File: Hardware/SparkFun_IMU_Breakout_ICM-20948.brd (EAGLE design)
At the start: 25.4 x 25.4 mm, 102 parts, among them Q1 DMN2005LP4K-7, Q10 RE1C002UN, Q11 DMN2005LP4K-7, Q12 RE1C002UN, Q13 DMN2005LP4K-7, Q14 RE1C002UN, Q15 DMN2005LP4K-7, Q16 RE1C002UN, Q2 RE1C002UN, Q3 DMN2005LP4K-7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

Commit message: Laid out v30
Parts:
- removed Q1, Q11, Q13, Q15, Q3, Q5, Q7, Q9: DMN2005LP4K-7, new_fets:AP02001
- added U$28: (no value), SparkFun-Aesthetics:SFE_LOGO_FLAME_.1
- added U$49: (no value), buzzard_labels (1):M3
- added U$50, U$57: (no value), buzzard_labels (1):X0
- added U$51, U$58: (no value), buzzard_labels (1):Y1
- added U$52, U$59: (no value), buzzard_labels (1):Z2
- added U$60: (no value), buzzard_labels (1):G5
- added U$61: (no value), buzzard_labels (1):A4
- moved R25 96.4 mm to (8.89, 18.7)
- moved R19 96.1 mm to (14.0, 18.7)
- moved R21 95.3 mm to (16.5, 18.7)
- moved R20 93.9 mm to (16.5, 15.9), turned to 180 degrees
- moved R23 91.3 mm to (11.4, 18.7)
- moved Q14 89.8 mm to (11.4, 17.8)
- moved R22 89.6 mm to (11.4, 15.9), turned to 180 degrees
- moved Q10 87.3 mm to (14.0, 17.8)
- moved R24 87.0 mm to (8.89, 15.9), turned to 180 degrees
- moved Q16 86.3 mm to (8.89, 17.8)
- moved Q12 85.8 mm to (16.5, 17.8)
- moved R18 84.9 mm to (14.0, 15.9), turned to 180 degrees
- moved R17 66.2 mm to (11.4, 6.73), turned to 180 degrees
- moved Q8 62.9 mm to (11.4, 7.62), turned to 180 degrees
- moved R16 61.7 mm to (11.4, 9.53)
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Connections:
- net AUX_CL_VIN_JMP renamed N$4
- net AUX_DA_VIN_JMP renamed N$5
- net SCL/SCLK_VIN_JMP renamed N$2
- net SDA/SDI_VIN_JMP renamed N$3
- net !CS: no longer Q1.S
- net !CS!_VIN: no longer Q1.D
- net 1.8V: no longer Q1.G, Q11.G, Q13.G, Q15.G, Q3.G, Q5.G, Q7.G, Q9.G
- net AD0/SDO: no longer Q3.S
- net AD0/SDO_VIN: no longer Q3.D
- net AUX_CL: no longer Q11.S
- net AUX_CL_VIN: now also J4.5; no longer J4.3, Q11.D
- net AUX_DA: no longer Q9.S
- net AUX_DA_VIN: now also J4.4; no longer J4.2, Q9.D
- net FSYNC: no longer Q13.S
- net FSYNC_VIN: now also J4.3; no longer J4.4, Q13.D
- net INT: no longer Q15.S
- net INT_VIN: now also J4.2; no longer J4.5, Q15.D
- net SCL/SCLK: no longer Q5.S
- net SCL/SCLK_VIN: no longer Q5.D
- net SDA/SDI: no longer Q7.S
- net SDA/SDI_VIN: no longer Q7.D
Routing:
- net VIN: track 0.00 -> 69.9 mm, vias 0 -> 11
- net 1.8V: track 0.00 -> 55.1 mm, vias 0 -> 11
- net SCL/SCLK_VIN: track 0.00 -> 41.8 mm, vias 0 -> 2
- net SDA/SDI_VIN: track 0.00 -> 41.4 mm, vias 0 -> 2
- net AUX_DA: track 0.00 -> 11.2 mm, vias 0 -> 2
- net AD0/SDO_VIN: track 0.00 -> 11.1 mm, vias 0 -> 2
- net !CS: track 0.00 -> 8.62 mm, vias 0 -> 2
- net AD0/SDO: track 0.00 -> 8.21 mm, vias 0 -> 2
- net !CS!_VIN: track 0.00 -> 7.80 mm, vias 0 -> 1
- net FSYNC_VIN: track 0.00 -> 7.78 mm, vias 0 -> 1
- net INT_VIN: track 0.00 -> 7.47 mm, vias 0 -> 1
- net AUX_DA_VIN: track 0.00 -> 7.37 mm, vias 0 -> 1
- net AUX_CL_VIN: track 0.00 -> 7.25 mm, vias 0 -> 1
- net GND: track 0.00 -> 6.58 mm, vias 0 -> 16
- net SDA/SDI: track 0.00 -> 5.65 mm, vias 0 -> 2
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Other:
- board text added: "v30"
- board text removed: "v21"

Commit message: Ran board design checklist ahead of the review
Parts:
- Q10, Q12, Q14, Q16, Q2, Q4, Q6, Q8: value RE1C002UN -> 20V/0.2A/8MHz/1.2Ω/1Vth; device new_fets:SOT-416FL -> SparkFun-DiscreteSemi:SOT-416FL
- moved U$37 0.40 mm to (4.78, 19.9)
- moved U$38 0.40 mm to (5.79, 19.9)
- moved U$24 0.13 mm to (6.35, 19.8)

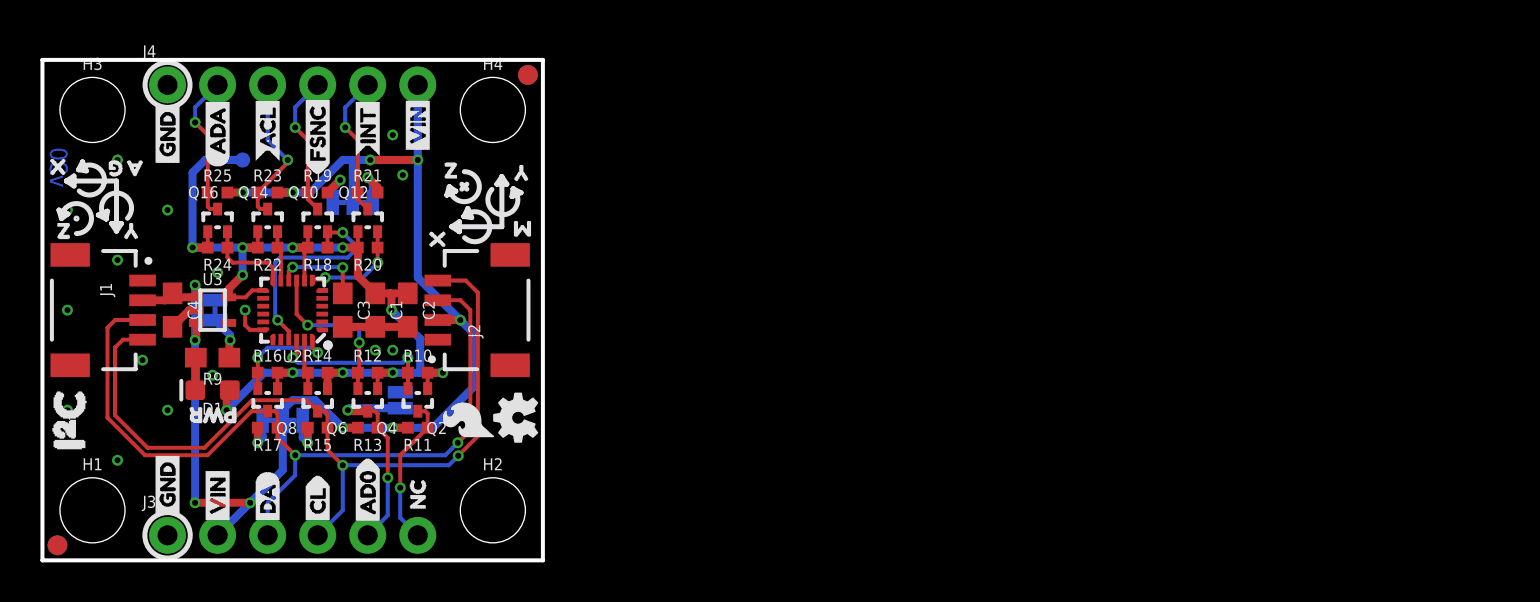
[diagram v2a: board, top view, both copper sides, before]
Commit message: Changes from design review
Level shifter circuit spacing
Axes indicators
Routing touch-ups
LED resistor change
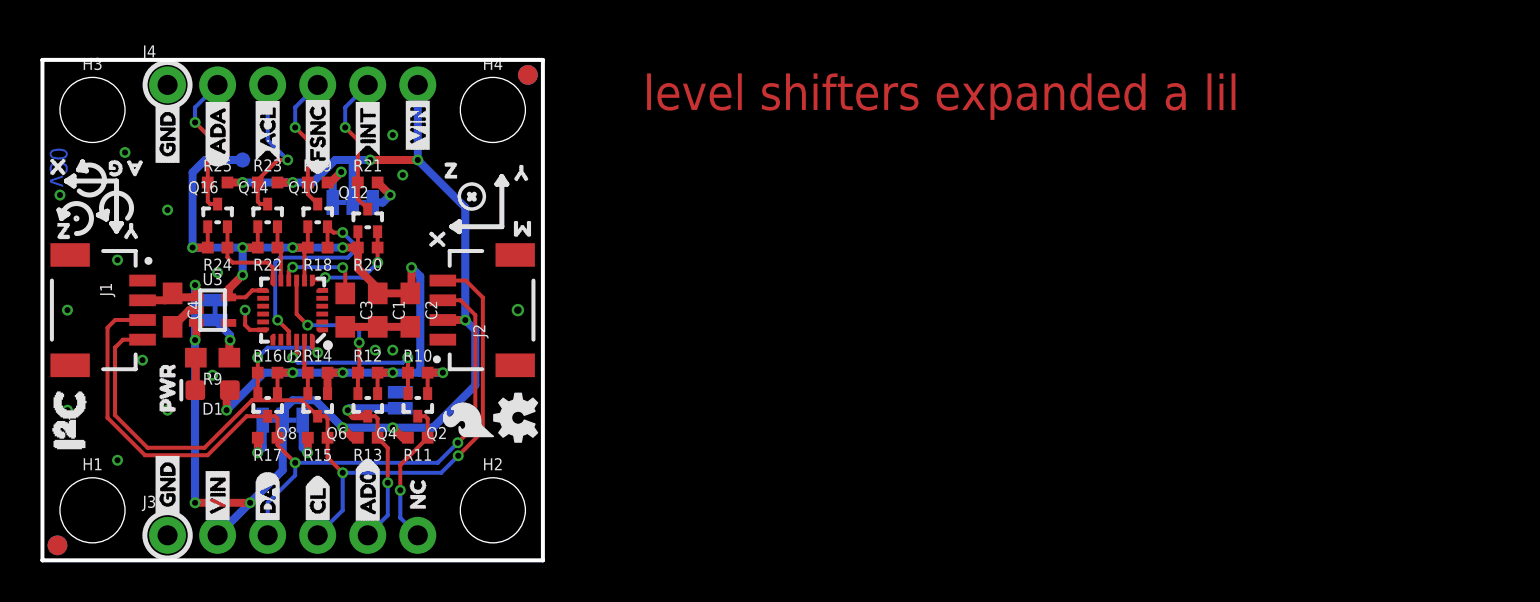
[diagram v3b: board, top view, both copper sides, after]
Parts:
- R9: value 470 -> 220
- moved U$3 4.22 mm to (6.35, 6.86), turned to 90 degrees
- moved R11 0.51 mm to (19.1, 6.22)
- moved R13 0.51 mm to (16.5, 6.22)
- moved R15 0.51 mm to (14.0, 6.22)
- moved R17 0.51 mm to (11.4, 6.22)
- moved R19 0.51 mm to (14.0, 19.2)
- moved R21 0.51 mm to (16.5, 19.2)
- moved R23 0.51 mm to (11.4, 19.2)
- moved R25 0.51 mm to (8.89, 19.2)
- moved J2 0.25 mm to (20.3, 12.7)
- moved Q2 0.25 mm to (19.1, 7.37)
- moved Q4 0.25 mm to (16.5, 7.37)
- moved Q6 0.25 mm to (14.0, 7.37)
- moved Q8 0.25 mm to (11.4, 7.37)
- moved Q10 0.25 mm to (14.0, 18.0)
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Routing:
- net 1.8V: track 55.1 -> 59.1 mm
- net N$3: track 2.01 -> 2.52 mm
- net N$2: track 2.01 -> 2.52 mm
- net GND: vias 16 -> 17
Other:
- board text added: "level shifters expanded a lil"
